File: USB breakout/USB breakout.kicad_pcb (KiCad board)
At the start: 2 copper layers, 31.5 x 16.2 mm, 11 parts, among them J1 USB_B_Micro, J2 Conn_01x06_Female

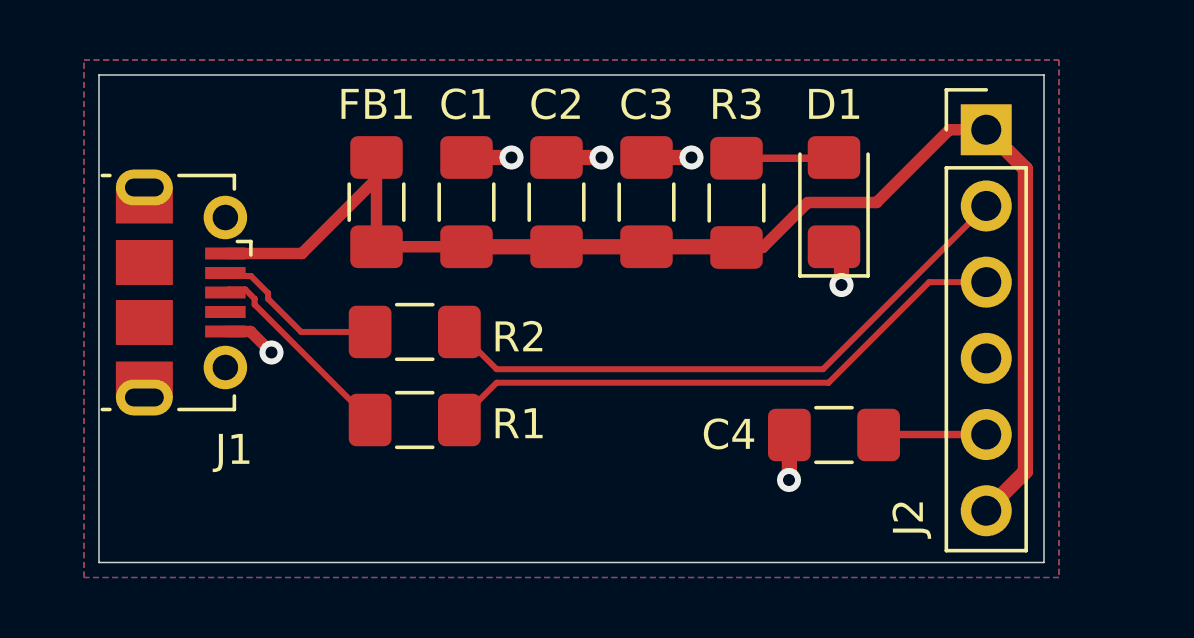
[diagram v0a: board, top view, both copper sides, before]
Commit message: Add labels, change header
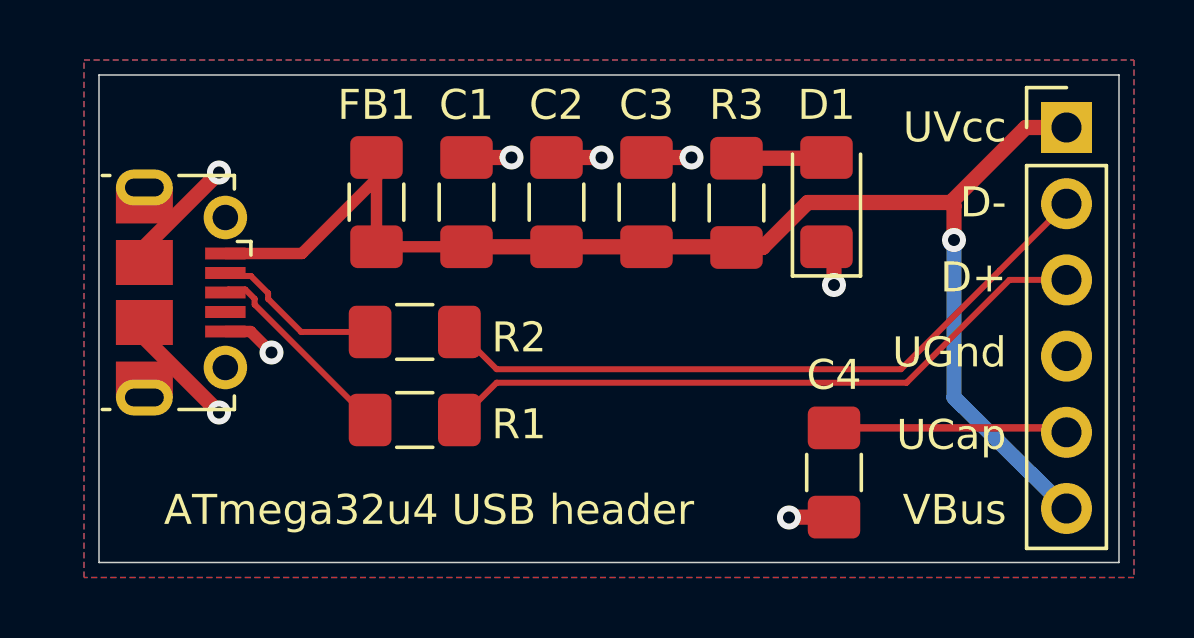
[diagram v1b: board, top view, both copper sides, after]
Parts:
- moved J2 2.68 mm to (132.2, 85.5)
- moved C4 1.25 mm to (124.5, 97.0), turned to 90 degrees
- moved D1 0.25 mm to (124.2, 88.0)
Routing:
- net UGnd: track 9.11 -> 17.2 mm, vias 6 -> 8
- net UCap: track 3.59 -> 7.81 mm
- net D+: track 19.5 -> 22.2 mm
- net D-: track 20.3 -> 23.0 mm
- net UVcc: track 45.7 -> 46.6 mm, vias 0 -> 1
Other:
- board size 31.5 x 16.2 mm -> 34 x 16.2 mm
- board text added: "ATmega32u4 USB header"
- board text added: "D+"
- board text added: "D-"
- board text added: "Solder header this side"
- board text added: "UCap"
- board text added: "UGnd"
- board text added: "UVcc"
- board text added: "VBus"

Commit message: Swap to different USB footprint
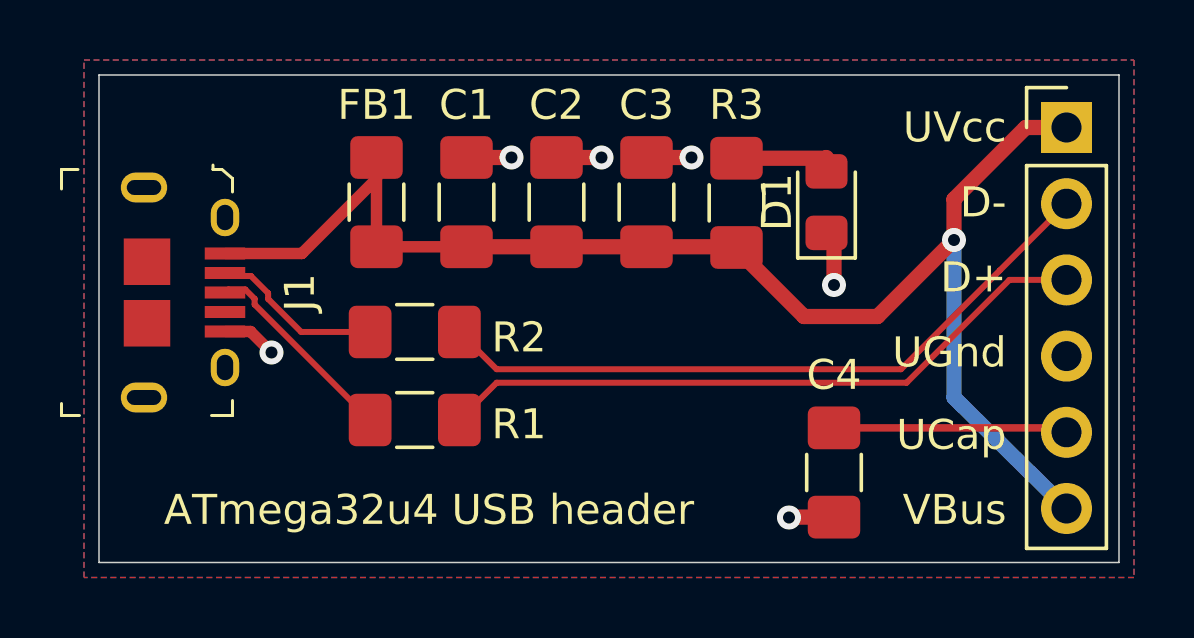
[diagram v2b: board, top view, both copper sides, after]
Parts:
- D1: footprint LED_SMD:LED_1206_3216Metric_Pad1.42x1.75mm_HandSolder -> LED_SMD:LED_0805_2012Metric_Pad1.15x1.40mm_HandSolder
- J1: footprint Connector_USB:USB_Micro-B_Molex-105017-0001 -> digikey-footprints:USB_Micro_B_Female_10118194-0001LF
- moved J1 1.45 mm to (104.2, 91.0)
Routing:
- net UGnd: track 17.2 -> 9.38 mm, vias 8 -> 6
- net UVcc: track 46.6 -> 48.1 mm

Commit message: Upsize all the connectors
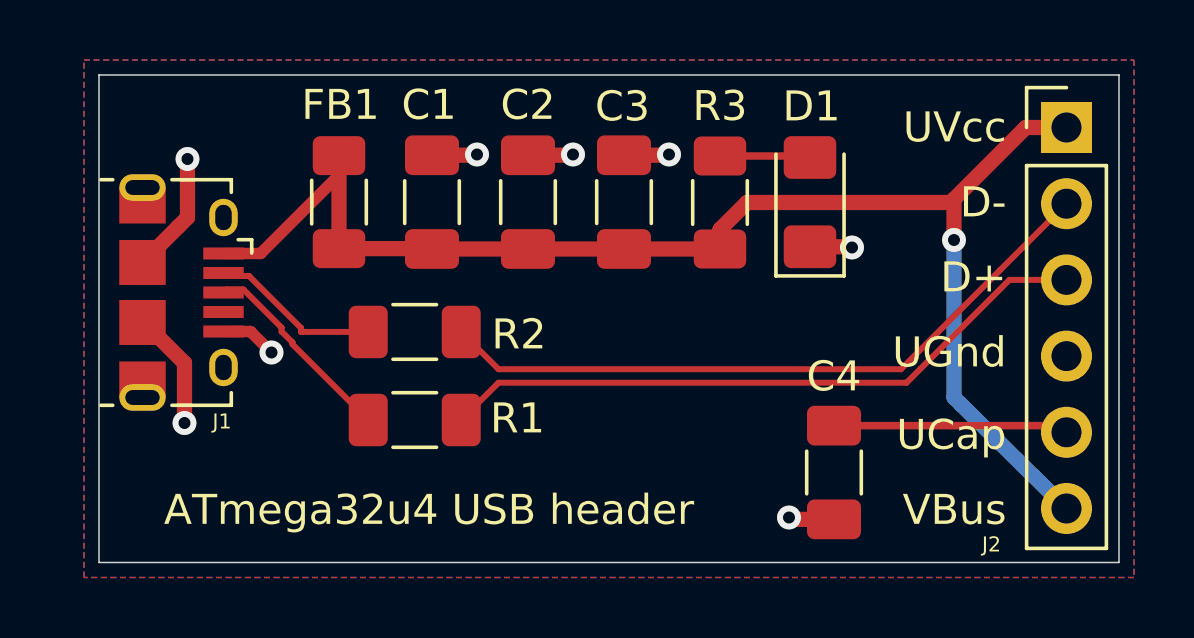
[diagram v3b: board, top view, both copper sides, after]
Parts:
- C1, C2, C3, C4: footprint Capacitor_SMD:C_1206_3216Metric_Pad1.42x1.75mm_HandSolder -> Capacitor_SMD:C_1206_3216Metric_Pad1.33x1.80mm_HandSolder
- D1: footprint LED_SMD:LED_0805_2012Metric_Pad1.15x1.40mm_HandSolder -> LED_SMD:LED_1206_3216Metric_Pad1.42x1.75mm_HandSolder
- FB1, R1, R2, R3: footprint Resistor_SMD:R_1206_3216Metric_Pad1.42x1.75mm_HandSolder -> Resistor_SMD:R_1206_3216Metric_Pad1.30x1.75mm_HandSolder
- J1: footprint digikey-footprints:USB_Micro_B_Female_10118194-0001LF -> Connector_USB:USB_Micro-B_Amphenol_10118194_Horizontal
- moved J1 1.45 mm to (102.8, 91.0)
- moved FB1 1.25 mm to (108.0, 88.0)
- moved C1 1.15 mm to (111.1, 88.0)
- moved C2 0.95 mm to (114.3, 88.0)
- moved C3 0.75 mm to (117.5, 88.0)
- moved R3 0.55 mm to (120.7, 88.0)
- moved D1 0.55 mm to (123.7, 88.0)
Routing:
- net UGnd: track 9.38 -> 17.6 mm, vias 6 -> 8
- net UVcc: track 48.1 -> 47.0 mm

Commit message: Final gerbers for USB breakout board
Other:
- rule pad_to_mask_clearance: 0.051 -> 0

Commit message: Breakout board and tbm930 board updates
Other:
- board text added: "JLCJLCJLCJLC"
